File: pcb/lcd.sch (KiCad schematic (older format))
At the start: 32 parts, among them J500 FPC_18P_1.0MM, U100 MCIMX7S5EVM08SC, U500 XC2C32A_QF32, U501 LT1617, U502 LM324

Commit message: pcb: rev 0.1
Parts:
- removed C504, C505, C506: 220nF, Capacitor_SMD:C_0402_1005Metric, symbol Device:C
- removed C507: 2.2uF, Capacitor_SMD:C_0402_1005Metric, symbol Device:C
- removed RN500, RN501: 33R, Resistor_SMD:R_Array_Convex_4x0402, symbol Device:R_Pack04
- removed U100: MCIMX7S5EVM08SC, footprints:BGA-541_25x25_19.0x19.0mm, symbol symbols:MCIMX7S5EVM08SC
- removed U500: XC2C32A_QF32, Package_DFN_QFN:QFN-32-1EP_5x5mm_P0.5mm_EP3.1x3.1mm, symbol symbols:XC2C32A_QF32
- added D500: MBR0530, Diode_SMD:D_SOD-123, symbol Device:D_Schottky
- added L502: 10uH, Inductor_SMD:L_Vishay_IHLP-1212, symbol Device:L
- added R510: 91K, Resistor_SMD:R_0603_1608Metric, symbol Device:R
- added R511: 30K, Resistor_SMD:R_0603_1608Metric, symbol Device:R
- added U500: LT1615, Package_TO_SOT_SMD:TSOT-23-5, symbol symbols:LT1615
- added U503: TXS0108EPW, Package_SO:TSSOP-20_4.4x6.5mm_P0.65mm, symbol symbols:TXS0108EPW
- C500, C501: value 100nF -> 10uF; footprint Capacitor_SMD:C_0402_1005Metric -> Capacitor_SMD:C_0603_1608Metric
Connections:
- net labels added: +5V, STN_CP, STN_CPG, STN_CPL, STN_D0, STN_D1, STN_FR, STN_S, STN_ST
- net labels removed: BT_CFG_1, BT_CFG_10, BT_CFG_11, BT_CFG_12, BT_CFG_13, BT_CFG_14, BT_CFG_2, BT_CFG_3, BT_CFG_4, BT_CFG_5, BT_CFG_6, CPLD_JTAG_TCK, CPLD_JTAG_TDI, CPLD_JTAG_TDO, CPLD_JTAG_TMS, HOLD, LCD_ARM_CLK, LCD_ARM_D6, LCD_ARM_D7, LCD_ARM_EN, LCD_ARM_HSYNC, LCD_ARM_VSYNC, LCD_RESET, QSPI_D0, QSPI_D1, QSPI_D2, QSPI_D3, QSPI_SCLK, SW_A, SW_B, SW_DN, SW_LE, SW_RI, SW_SE, SW_ST, SW_UP, ~QSPI_SS0
- wire segments 189 -> 128
- no-connect marks 29 -> 0
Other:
- note removed: "TFT to STN Bridge"
- moved on the sheet: C508, C510, C512, D501, J500, L500, L501, R501, R503, R504, R505, R506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

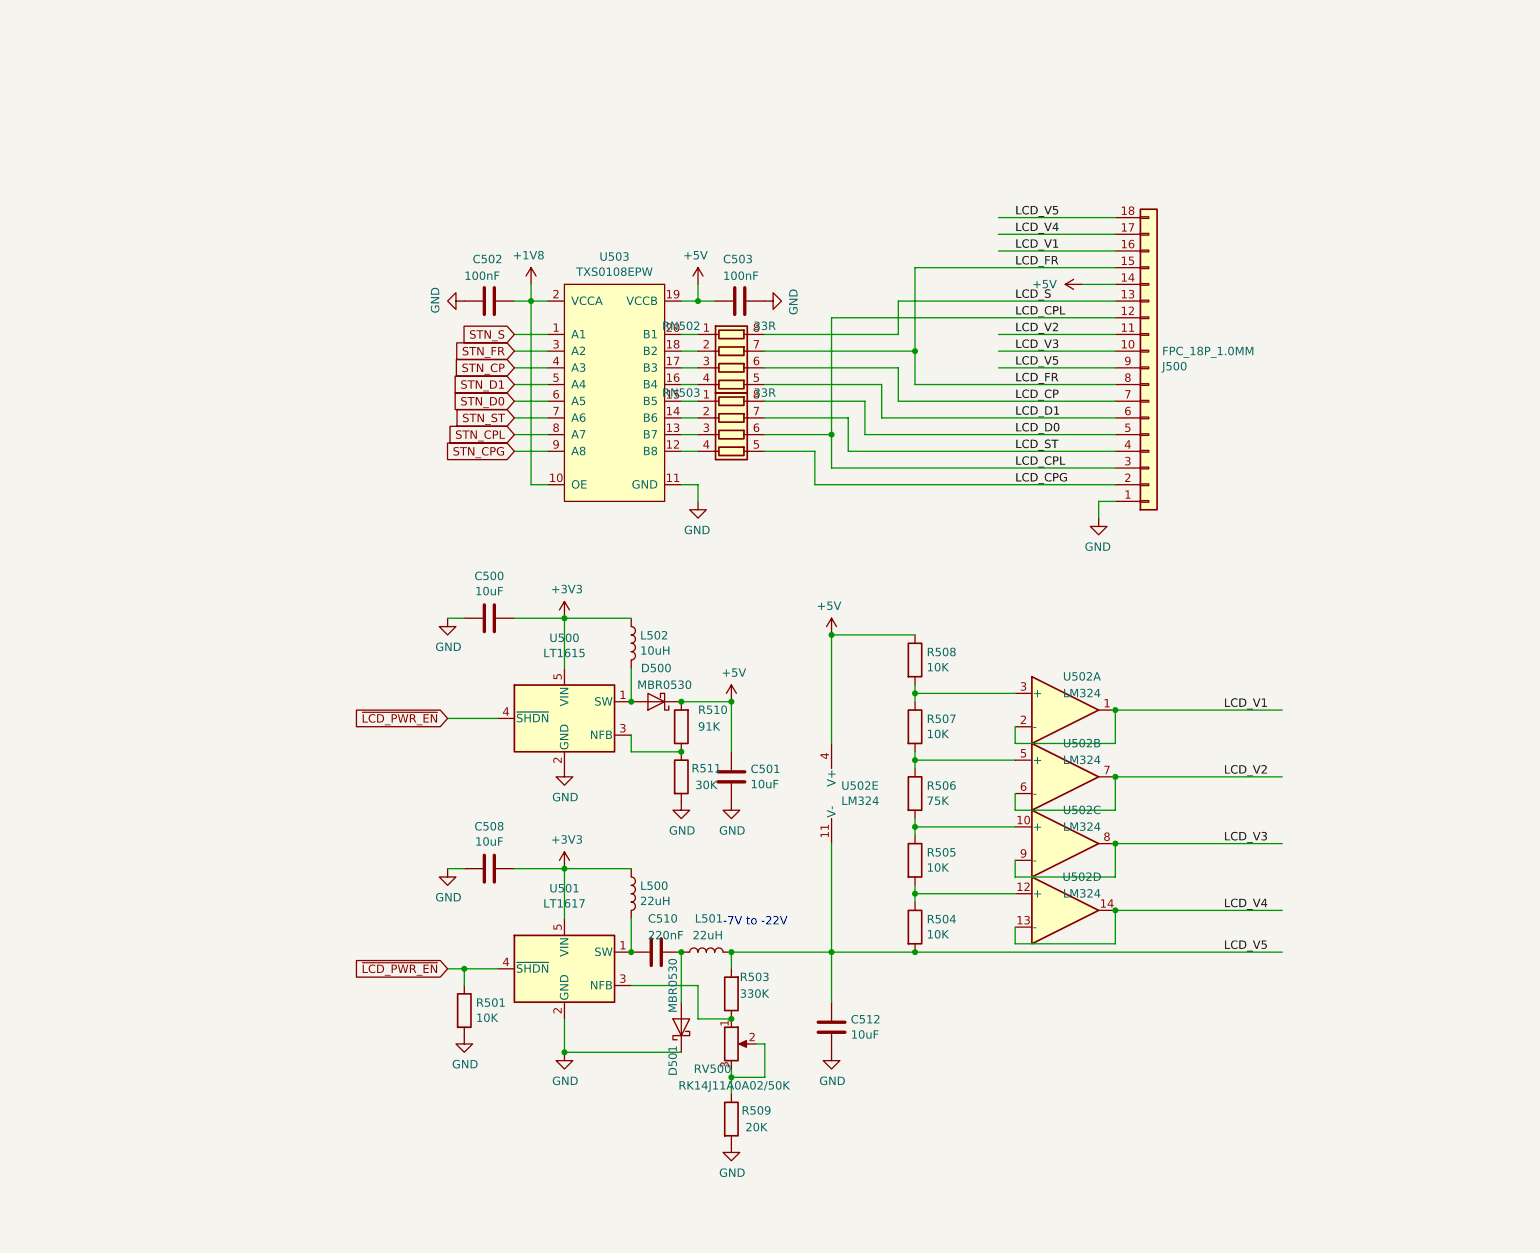
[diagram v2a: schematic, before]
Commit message: pcb: fixing i2c numbering; add filtering for lcd
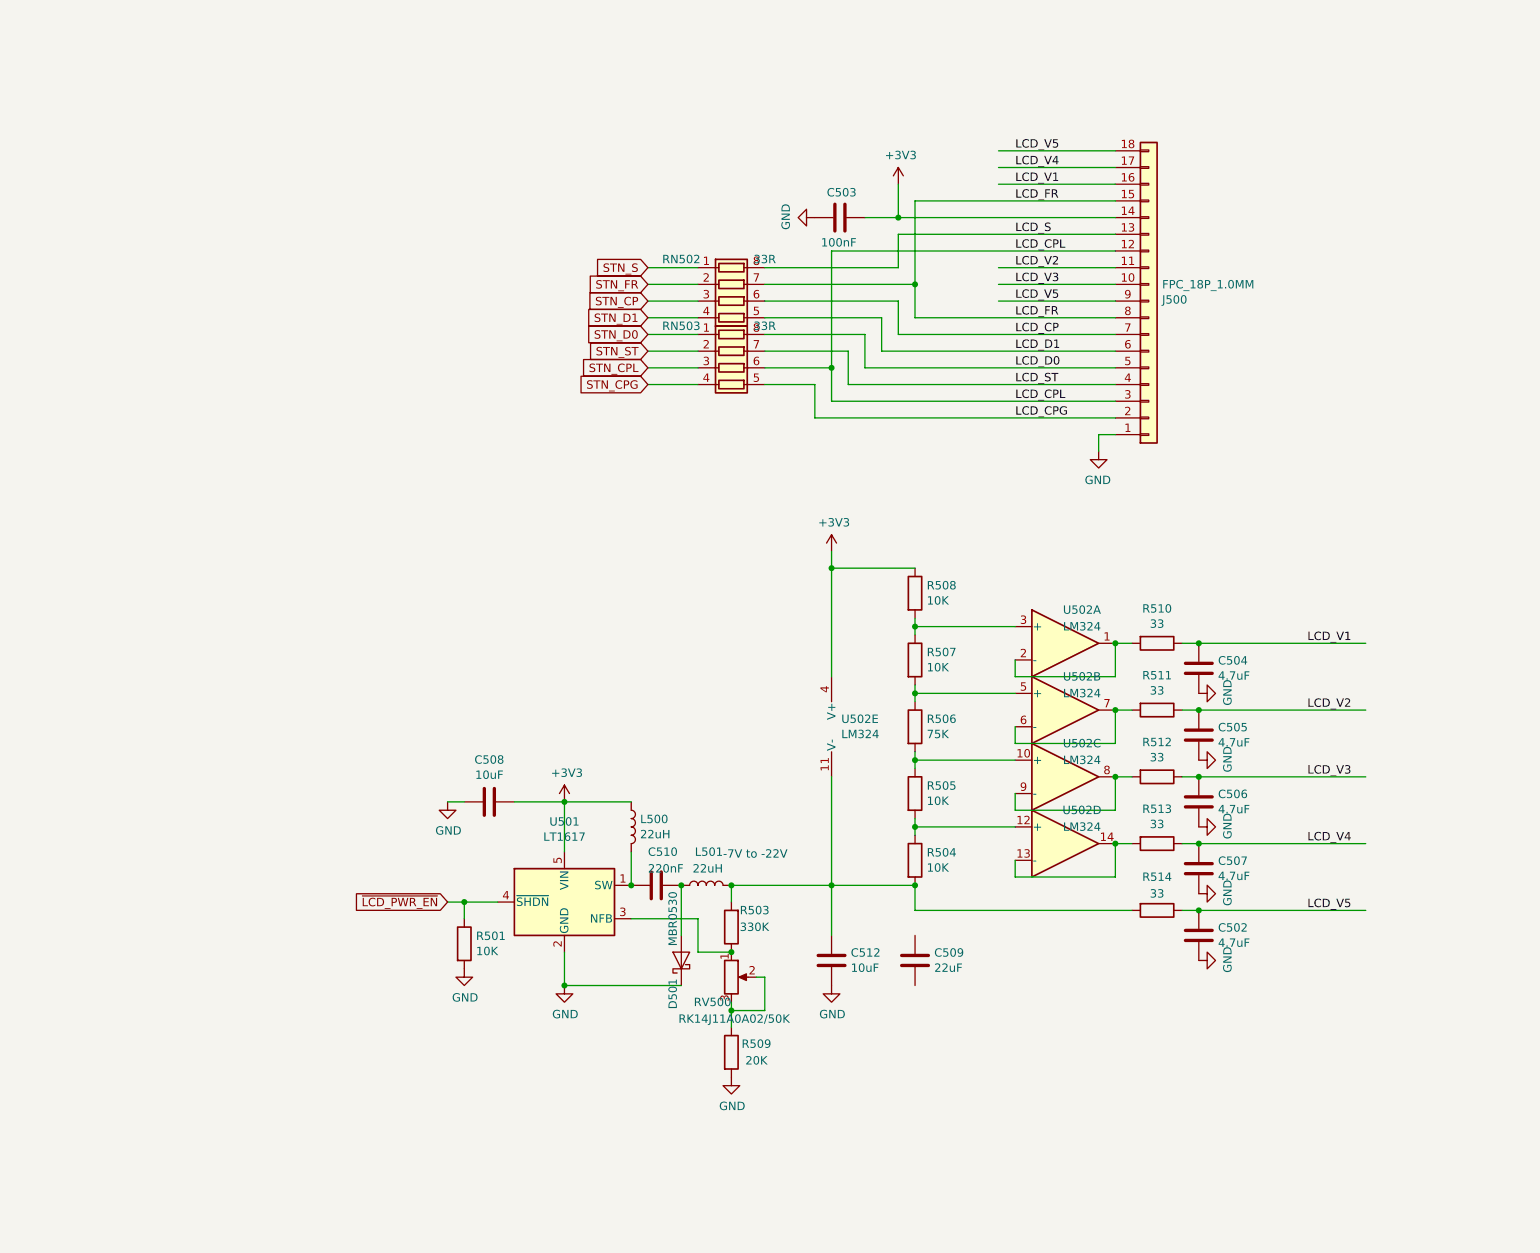
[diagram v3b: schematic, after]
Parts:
- removed C500, C501: 10uF, Capacitor_SMD:C_0603_1608Metric, symbol Device:C
- removed D500: MBR0530, Diode_SMD:D_SOD-123, symbol Device:D_Schottky
- removed L502: 10uH, Inductor_SMD:L_Vishay_IHLP-1212, symbol Device:L
- removed U500: LT1615, Package_TO_SOT_SMD:TSOT-23-5, symbol symbols:LT1615
- removed U503: TXS0108EPW, Package_SO:TSSOP-20_4.4x6.5mm_P0.65mm, symbol symbols:TXS0108EPW
- added C504, C505, C506, C507: 4.7uF, Capacitor_SMD:C_0603_1608Metric, symbol Device:C
- added C509: 22uF, Capacitor_SMD:C_1206_3216Metric, symbol Device:C
- added R512, R513, R514: 33, Resistor_SMD:R_0603_1608Metric, symbol Device:R
- C502: value 100nF -> 4.7uF; footprint Capacitor_SMD:C_0402_1005Metric -> Capacitor_SMD:C_0603_1608Metric
- R510: value 91K -> 33
- R511: value 30K -> 33
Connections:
- net labels removed: +1V8, +5V
- wire segments 128 -> 114
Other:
- moved on the sheet: C503, C508, C510, C512, D501, J500, L500, L501, R501, R503, R504, R505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

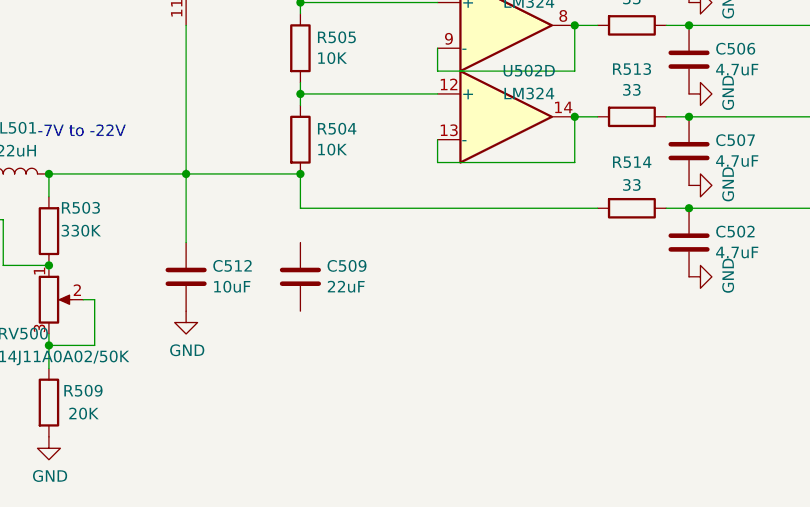
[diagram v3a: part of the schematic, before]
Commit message: pcb: use crystal instead
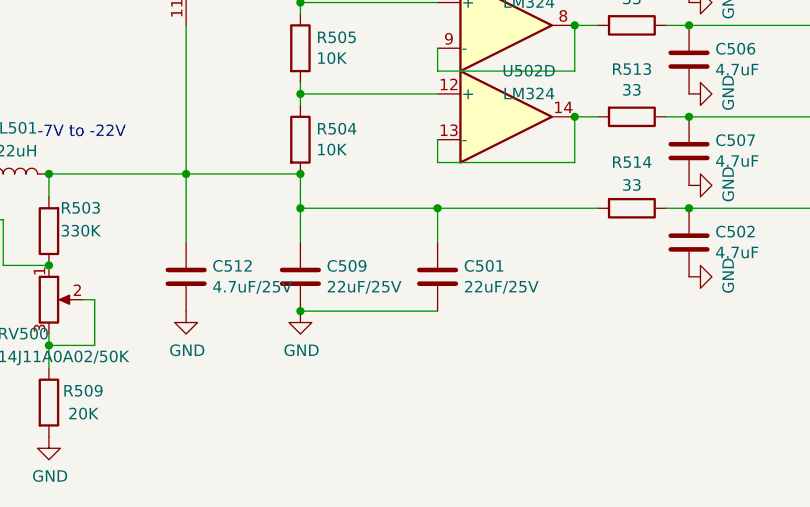
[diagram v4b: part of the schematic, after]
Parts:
- added C501: 22uF/25V, Capacitor_SMD:C_1206_3216Metric, symbol Device:C
- C509: value 22uF -> 22uF/25V
- C512: value 10uF -> 4.7uF/25V
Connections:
- wire segments 114 -> 118
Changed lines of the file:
@@
 P 6200 6150
 F 0 "C512" H 6085 6104 50  0000 R CNN
-F 1 "10uF" H 6085 6195 50  0000 R CNN
+F 1 "4.7uF/25V" H 6085 6195 50  0000 R CNN
 F 2 "Capacitor_SMD:C_0603_1608Metric" H 6238 6000 50  0001 C CNN
 F 3 "~" H 6200 6150 50  0001 C CNN
@@
 Connection ~ 7900 5450
 Wire Wire Line
-	8000 5850 6700 5850
+	8000 5850 7300 5850
 Wire Wire Line
 	6700 5850 6700 5700
@@
 AR Path="/5DB51F59/5DBE7291" Ref="C509"  Part="1"
 F 0 "C509" H 6815 6196 50  0000 L CNN
-F 1 "22uF" H 6815 6105 50  0000 L CNN
+F 1 "22uF/25V" H 6815 6105 50  0000 L CNN
 F 2 "Capacitor_SMD:C_1206_3216Metric" H 6738 6000 50  0001 C CNN
 F 3 "~" H 6700 6150 50  0001 C CNN
@@
 	1    0    0    -1
 $EndComp
+Wire Wire Line
+	6700 6000 6700 5850
+Connection ~ 6700 5850
+$Comp
+L power:GND #PWR?
+U 1 1 5DB7C3CC
+P 6700 6300
+AR Path="/5DB2122B/5DB7C3CC" Ref="#PWR?"  Part="1"
+AR Path="/5DB51F59/5DB7C3CC" Ref="#PWR0141"  Part="1"
+F 0 "#PWR0141" H 6700 6050 50  0001 C CNN
+F 1 "GND" H 6705 6127 50  0000 C CNN
+F 2 "" H 6700 6300 50  0001 C CNN
+F 3 "" H 6700 6300 50  0001 C CNN
+	1    6700 6300
+	1    0    0    -1
+$EndComp
+$Comp
+L Device:C C?
+U 1 1 5DB8753F
+P 7300 6150
+AR Path="/5D4C99F9/5DB8753F" Ref="C?"  Part="1"
+AR Path="/5DB51F59/5DB8753F" Ref="C501"  Part="1"
+F 0 "C501" H 7415 6196 50  0000 L CNN
+F 1 "22uF/25V" H 7415 6105 50  0000 L CNN
+F 2 "Capacitor_SMD:C_1206_3216Metric" H 7338 6000 50  0001 C CNN
+F 3 "~" H 7300 6150 50  0001 C CNN
+	1    7300 6150
+	1    0    0    -1
+$EndComp
+Wire Wire Line
+	7300 6000 7300 5850
+Connection ~ 7300 5850
+Wire Wire Line
+	7300 5850 6700 5850
+Wire Wire Line
+	7300 6300 6700 6300
+Connection ~ 6700 6300
 $EndSCHEMATC
